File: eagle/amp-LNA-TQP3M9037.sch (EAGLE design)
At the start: 18 parts, among them J1 142-0701-851, J2 142-0701-851, U1 TQP3M903X

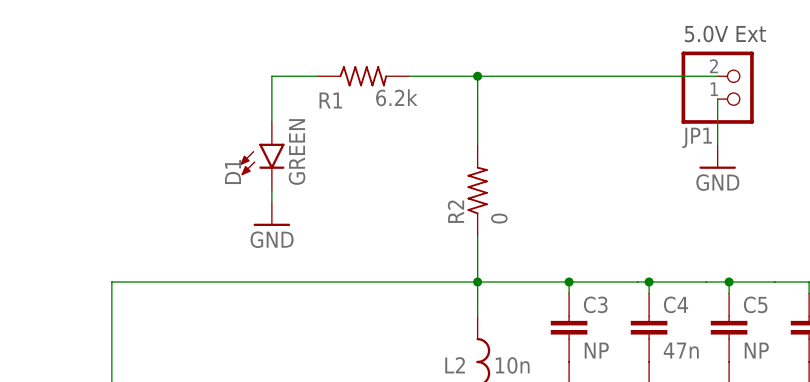
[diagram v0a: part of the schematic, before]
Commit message: lna-tqp3m9037 update values
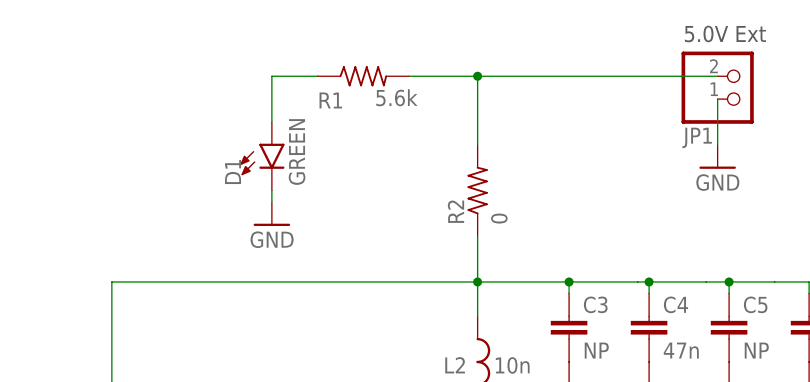
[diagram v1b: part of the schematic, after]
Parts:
- R1: value 6.2k -> 5.6k
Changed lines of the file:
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@@
 </part>
 <part name="GND80" library="supply1" deviceset="GND" device=""/>
-<part name="R1" library="oresat-rcl" deviceset="R-US_" device="0603-B-NOSILK" value="6.2k"/>
+<part name="R1" library="oresat-rcl" deviceset="R-US_" device="0603-B-NOSILK" value="5.6k"/>
 <part name="J1" library="J-Cinch-142-0701-851-SMA-end-launch" deviceset="142-0701-851" device=""/>
 <part name="J2" library="J-Cinch-142-0701-851-SMA-end-launch" deviceset="142-0701-851" device=""/>
